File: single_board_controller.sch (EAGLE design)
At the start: 74 parts, among them IC1 MCP3008, IC2 MCP3008, K1 AQ1AD2-3, K2 RELAY, P1 B9B-EH-A, P2 STEPPER, Q1 NPN, Q2 NPN, Q3 NPN, Q4 NPN, Q7 TRANSISTIOR, Q8 TRANSISTIOR, T1 BTA41, U1 OPTOISOLATOR-2SOIC8, U2 OPTOISOLATOR-2SOIC8, U4 OPTO-ISO

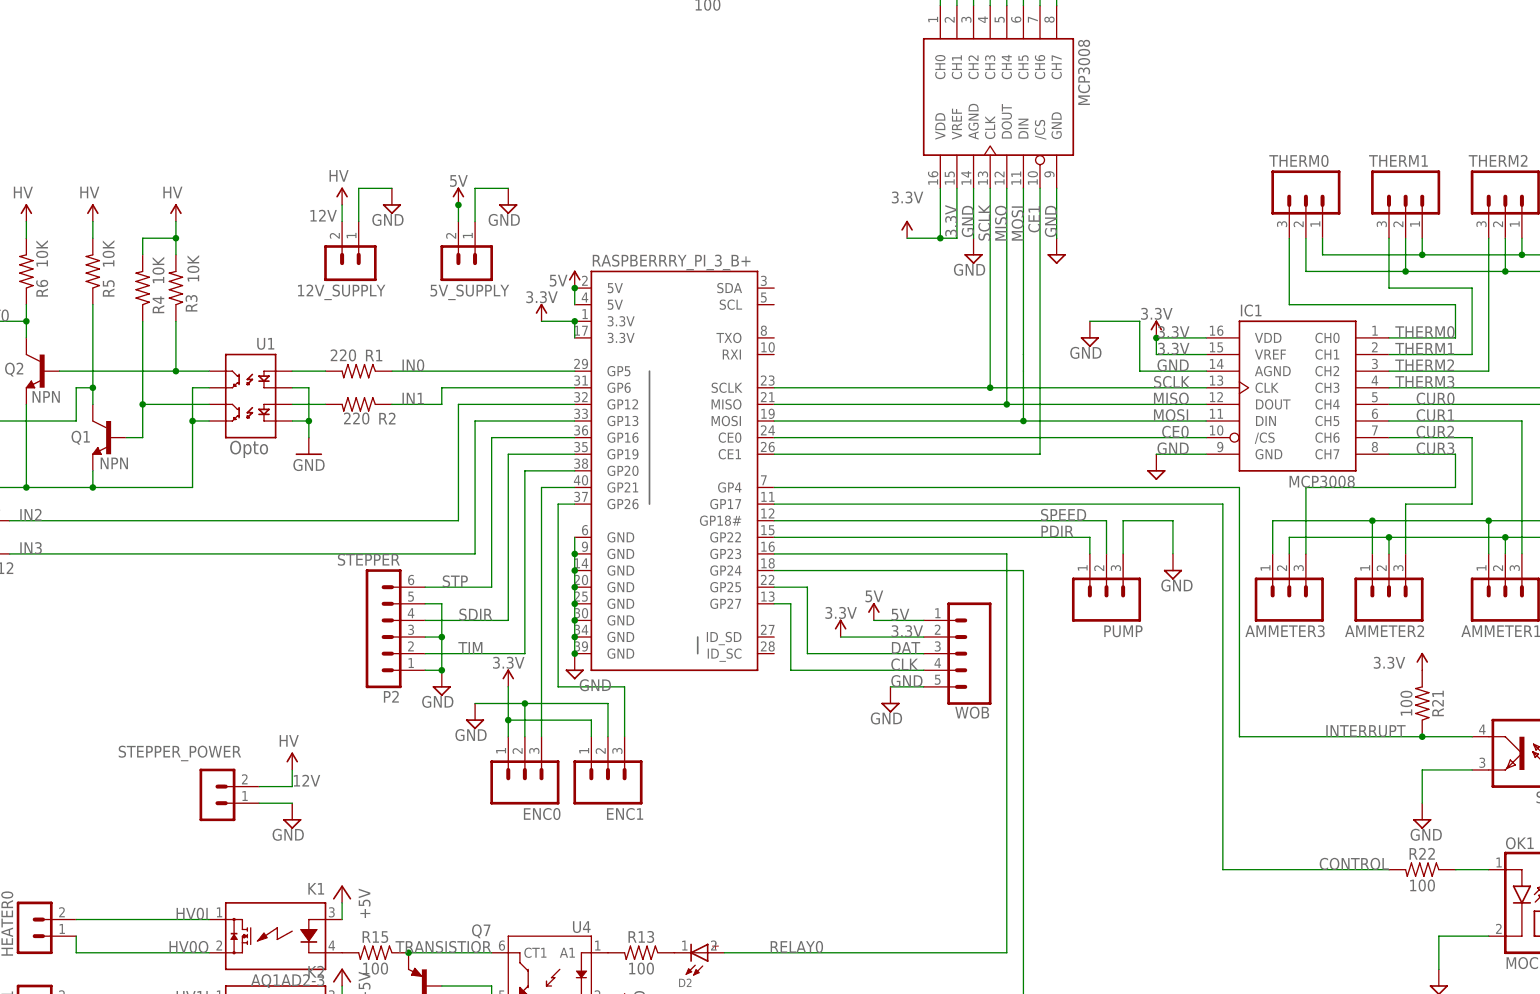
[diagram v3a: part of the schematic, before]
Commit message: added atiny85 drill driver, added mounting holes, isolated ground and 3.3V planes from AC, added I2C connector, still need to choose new mosfets, still need to verify AC circuitry, still need to pick appropriate resistors/capacitor/diodes
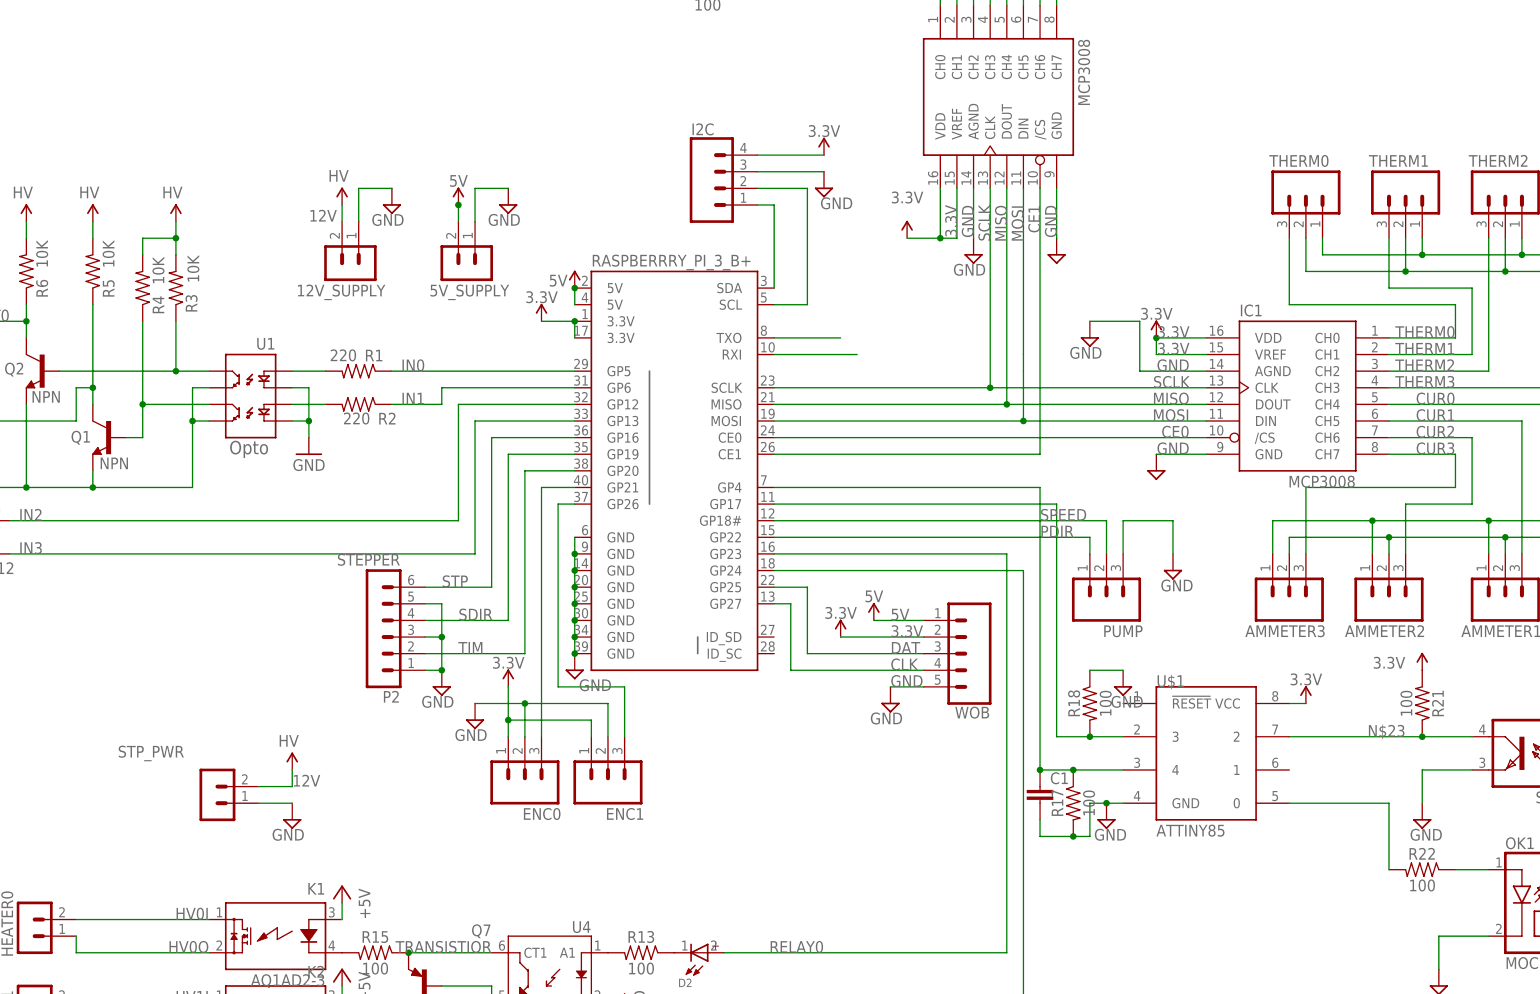
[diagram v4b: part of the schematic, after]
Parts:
- added C1: (no value), eagle-ltspice:C
- added I2C: (no value), SparkFun-Connectors:CONN_04JST-PTH-VERT
- added R17, R18: 100, SparkFun-Resistors:0.3OHM-0805-1/8W-1%
- added U$1: ATTINY85, attiny85:ATTINY85
- renumbered STEPPER_POWER to STP_PWR
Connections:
- removed net INTERRUPT: OK3.C, R21.1, RASPBERRRY_PI_3_B+.GP4
- new net N$23: OK3.C, R21.1, U$1.2
- new net N$27: R22.2, U$1.0
- new net N$28: I2C.2, RASPBERRRY_PI_3_B+.SCL
- new net N$29: C1.1, R17.1, RASPBERRRY_PI_3_B+.GP4, U$1.4
- new net N$30: I2C.1, RASPBERRRY_PI_3_B+.SDA
- new net N$31: RASPBERRRY_PI_3_B+.RXI
- new net N$32: RASPBERRRY_PI_3_B+.TXO
- net 3.3V: now also I2C.4, U$1.VCC
- net CONTROL: now also R18.2, U$1.3; no longer R22.2
- net GND: now also C1.2, I2C.3, R17.2, R18.1, U$1.GND

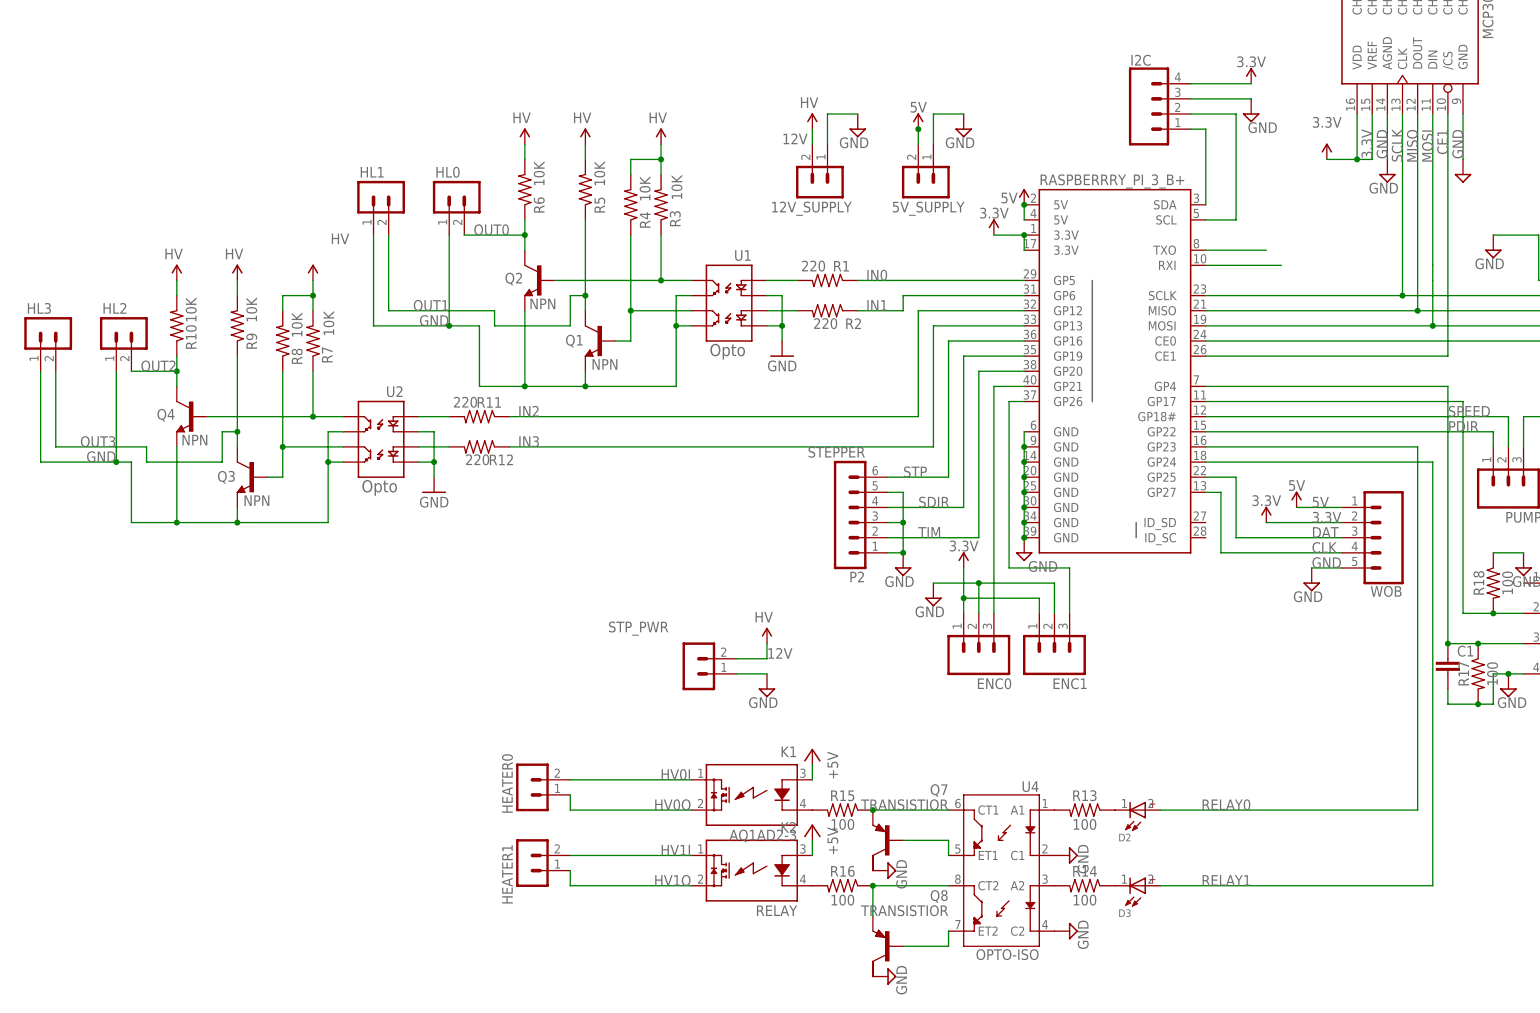
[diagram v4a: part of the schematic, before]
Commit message: in process of replacing components
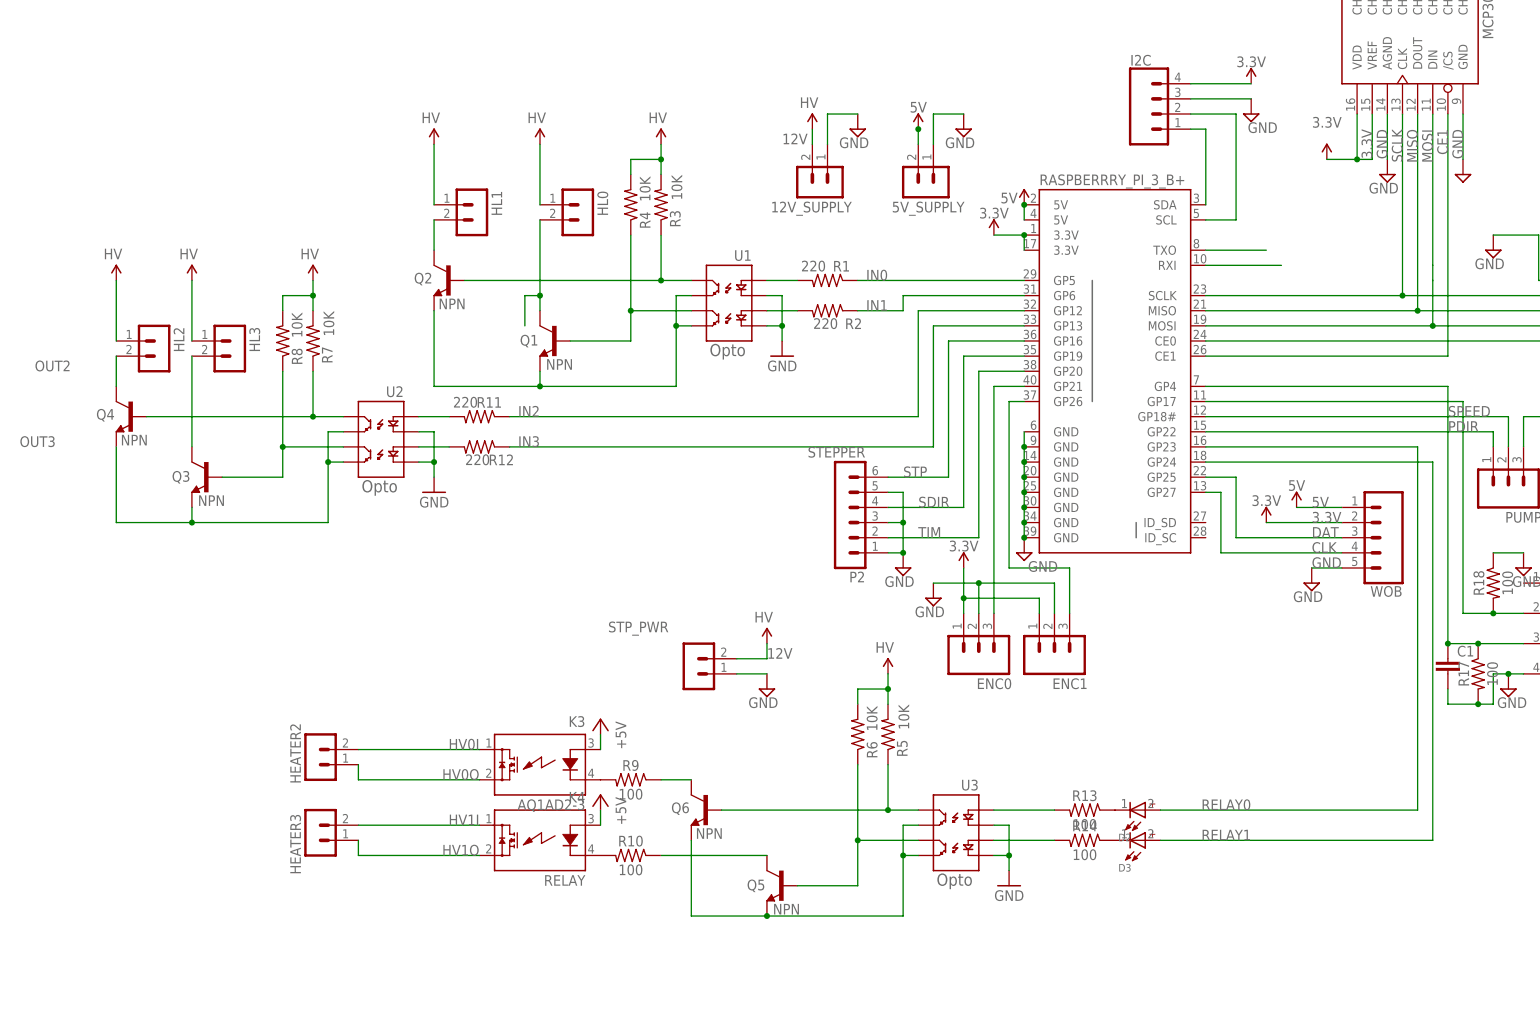
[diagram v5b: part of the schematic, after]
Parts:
- removed HEATER0, HEATER1: B2P-VH, con-jst-vh:B2P-VH
- removed K1: AQ1AD2-3, relay:AQ1AD2-3
- removed K2: RELAY, relay:AQ1AD2-3
- removed Q7, Q8: TRANSISTIOR, semicon-smd-ipc:PNP-TRANSISTIOR-2COLSOT89
- removed R15, R16: 100, SparkFun-Resistors:0.3OHM-0805-1/8W-1%
- removed U4: OPTO-ISO, SparkFun-DiscreteSemi:ILD213T-IDL213T
- added HEATER2, HEATER3: B2P-VH, con-jst-vh:B2P-VH
- added K3: AQ1AD2-3, relay:AQ1AD2-3
- added K4: RELAY, relay:AQ1AD2-3
- added Q5, Q6: NPN, SparkFun-DiscreteSemi:TRANSISTOR_NPNMMBT2222A
- added U3: OPTOISOLATOR-2SOIC8, SparkFun-DiscreteSemi:OPTOISOLATOR-2SOIC8
- R10, R9: value 10K -> 100; device SparkFun-Resistors:10KOHM1/10W1%(0603)0603 -> SparkFun-Resistors:0.3OHM-0805-1/8W-1%
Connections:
- removed net N$12: R13.2, U4.A1
- removed net N$14: R14.2, U4.A2
- removed net N$16: Q7.E, R15.1, U4.CT1
- removed net N$17: K1.K, R15.2
- removed net N$18: Q8.E, R16.1, U4.CT2
- removed net N$19: K2.K, R16.2
- removed net N$20: Q7.B, U4.ET1
- removed net N$21: Q8.B, U4.ET2
- new net N$22: R13.2, U3.A1
- new net N$33: R14.2, U3.A2
- new net N$34: K4.K, R10.2
- new net N$35: K3.K, R9.2
- new net N$36: Q6.C, R9.1
- new net N$37: Q5.C, R10.1
- new net OUT1N2: Q6.B, R5.1, U3.CL1
- new net OUT2N2: Q5.B, R6.1, U3.CL2
- net +5V: now also K3.A, K4.A; no longer K1.A, K2.A
- net 12V: now also HL0.1, HL1.1, HL2.1, HL3.1; no longer R10.2, R9.2
- net GND: now also Q5.E, Q6.E, U3.C1, U3.C2, U3.EM1, U3.EM2; no longer HL0.1, HL1.1, HL2.1, HL3.1, Q7.C, Q8.C, U4.C1, U4.C2
- net HV0I: now also HEATER2.2, K3.DS1; no longer HEATER0.2, K1.DS1
- net HV0O: now also HEATER2.1, K3.DS2; no longer HEATER0.1, K1.DS2
- net HV1I: now also HEATER3.2, K4.DS1; no longer HEATER1.2, K2.DS1
- net HV1O: now also HEATER3.1, K4.DS2; no longer HEATER1.1, K2.DS2
- net OUT0: now also HL1.2; no longer HL0.2, R6.1
- net OUT1: now also HL0.2; no longer HL1.2, R5.1
- net OUT2: no longer R10.1
- net OUT3: no longer R9.1
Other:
- moved on the sheet: D3, HL0, HL1, HL2, HL3, Q1, Q2, Q3, Q4, R10, R14, R5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

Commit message: already sent to fab, working on small improvements
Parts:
- removed K3: AQ1AD2-3, relay:AQ1AD2-3
- removed K4: RELAY, relay:AQ1AD2-3
- removed Q6: NPN, SparkFun-DiscreteSemi:TRANSISTOR_NPNMMBT2222A
- added -12V_SUPPLY: B2P-VH, con-jst-vh:B2P-VH
- added K1, K2: AQE12105, G6DN_relay:AQE12105
- added Q8: 35A/25V/8.5mΩ, SparkFun-DiscreteSemi:MOSFET-NCH-FDD8780
- Q1, Q2, Q3, Q4, Q5: value NPN -> 35A/25V/8.5mΩ; device SparkFun-DiscreteSemi:TRANSISTOR_NPNMMBT2222A -> SparkFun-DiscreteSemi:MOSFET-NCH-FDD8780
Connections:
- removed net HV0I: HEATER2.2, K3.DS1
- removed net HV0O: HEATER2.1, K3.DS2
- removed net HV1I: HEATER3.2, K4.DS1
- removed net HV1O: HEATER3.1, K4.DS2
- removed net N$24: B1.AC2, MAINS.1, R23.2, T1.A2
- removed net N$25: B1.AC1, DRILL.1, MAINS.2
- removed net N$34: K4.K, R10.2
- removed net N$35: K3.K, R9.2
- new net -12V: -12V_SUPPLY.2, STP_PWR.1
- new net MAINS-H: B1.AC2, HEATER2.2, HEATER3.2, MAINS.1, R23.2, T1.A2
- new net MAINS-N: B1.AC1, DRILL.1, K1.DS1, K2.DS1, MAINS.2
- new net N$12: HEATER2.1, K1.DS2
- new net N$14: K2.A, R10.2
- new net N$16: K1.A, R9.2
- new net N$17: HEATER3.1, K2.DS2
- new net VCC: U3.CL1, U3.CL2
- net +5V: now also K1.K, K2.K; no longer K3.A, K4.A
- net 12V: now also U1.CL1, U1.CL2, U2.CL1, U2.CL2; no longer R3.2, R4.2, R5.2, R6.2, R7.2, R8.2
- net GND: now also -12V_SUPPLY.1, Q1.S, Q2.S, Q3.S, Q4.S, Q5.S, Q8.S, R3.2, R4.2, R5.2, R6.2, R7.2, R8.2; no longer Q1.E, Q2.E, Q3.E, Q4.E, Q5.E, Q6.E, STP_PWR.1, U1.EM1, U1.EM2, U2.EM1, U2.EM2, U3.EM1, U3.EM2
- net N$36: now also Q5.D; no longer Q6.C
- net N$37: now also Q4.D; no longer Q5.C
- net OUT0: now also Q1.D; no longer Q2.C
- net OUT1: now also Q2.D; no longer Q1.C
- net OUT1N: now also Q1.G, U1.EM1; no longer Q2.B, U1.CL1
- net OUT1N1: now also Q3.G, U2.EM1; no longer Q4.B, U2.CL1
- net OUT1N2: now also Q5.G, U3.EM1; no longer Q6.B, U3.CL1
- net OUT2: now also Q3.D; no longer Q4.C
- net OUT2N: now also Q2.G, U1.EM2; no longer Q1.B, U1.CL2
- net OUT2N1: now also Q8.G, U2.EM2; no longer Q3.B, U2.CL2
- net OUT2N2: now also Q4.G, U3.EM2; no longer Q5.B, U3.CL2
- net OUT3: now also Q8.D; no longer Q3.C
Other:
- moved on the sheet: HEATER2, HEATER3
